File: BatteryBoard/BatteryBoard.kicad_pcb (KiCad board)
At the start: 4 copper layers, 45 x 44 mm, 67 parts, among them J1 M55-7102642R, Q1 PMPB13XNE,115, Q2 PMPB13XNE,115, Q3 PMPB13XNE,115, Q5 PMPB13XNE,115, U1 INA185A4IDRLR, U10 SI3477DV-T1-GE3, U13 TPS259472ARPWR, U2 SI3477DV-T1-GE3, U6 TPS63802DLAR, U8 BQ25756ERRVR

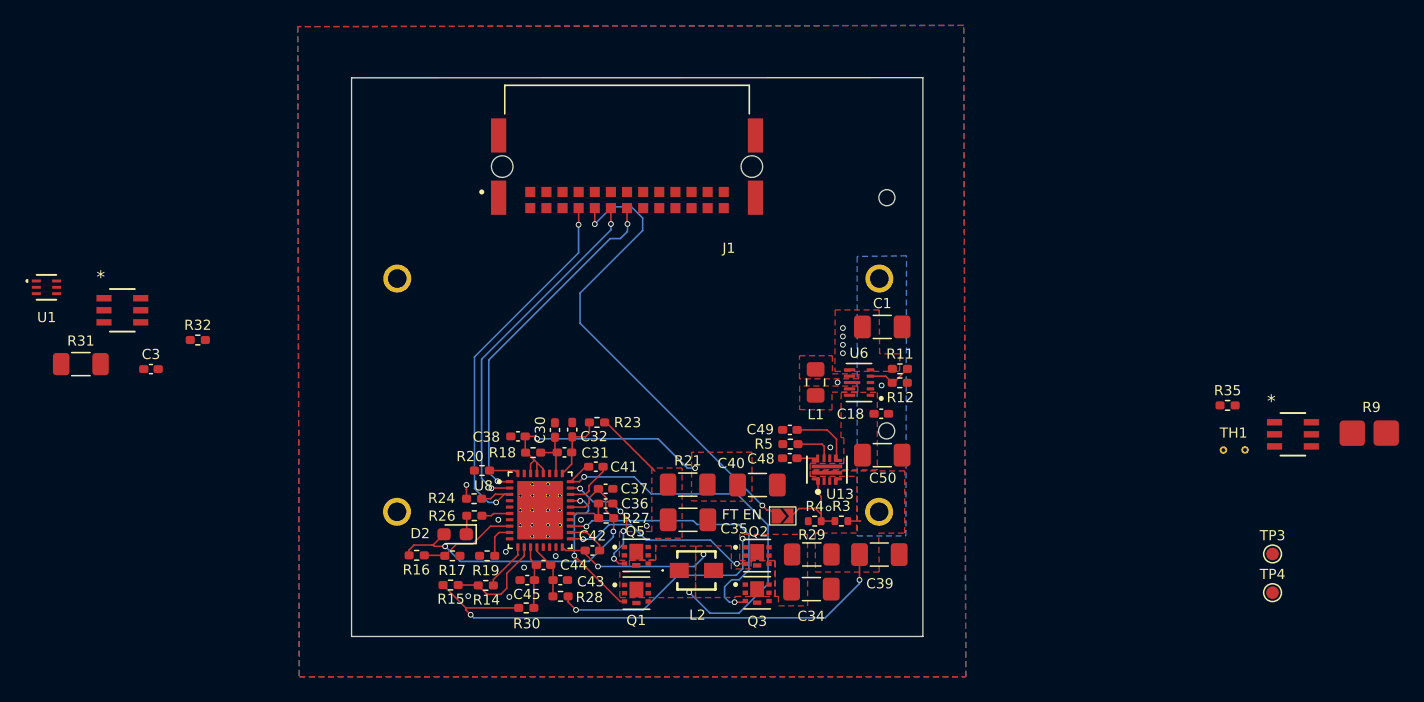
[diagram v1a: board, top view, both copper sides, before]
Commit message: Routing and schematic work on most boards
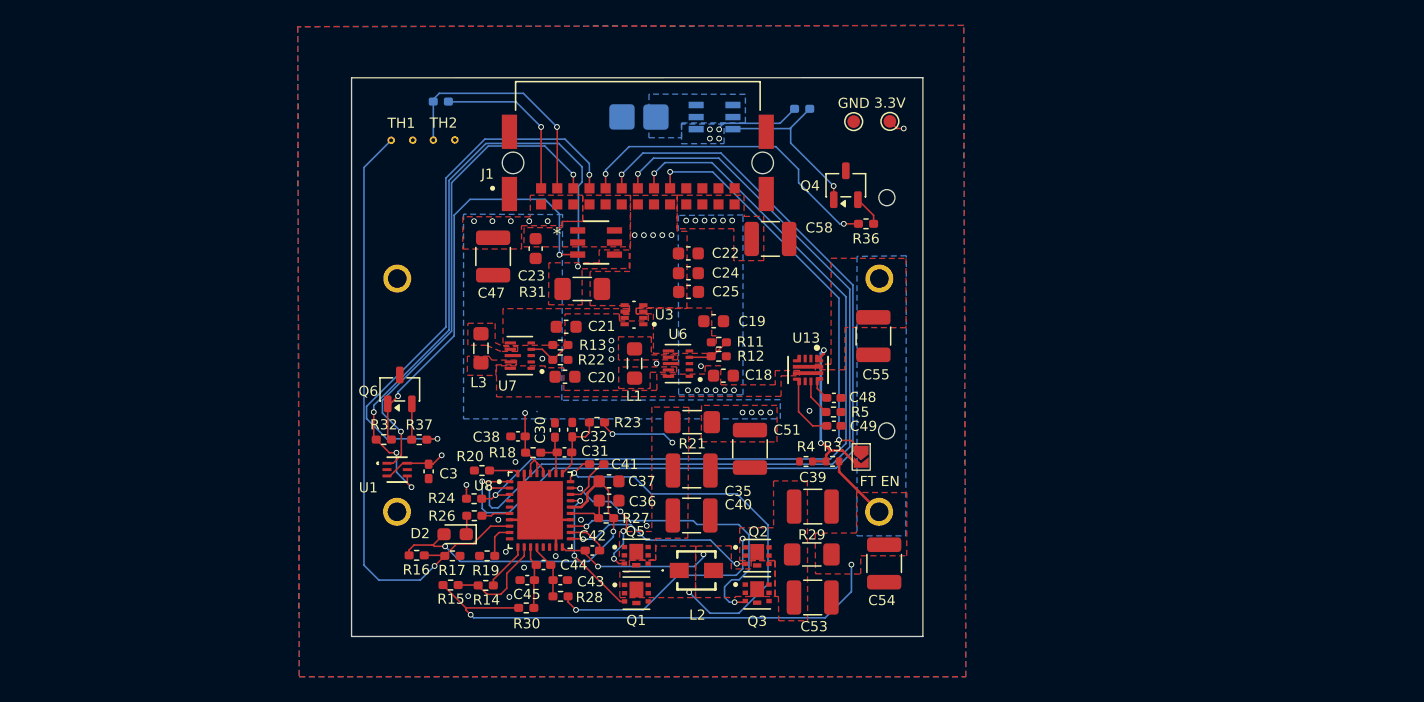
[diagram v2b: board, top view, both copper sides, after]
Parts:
- removed C1, C34, C50: 47uF, Capacitor_SMD:C_1206_3216Metric_Pad1.33x1.80mm_HandSolder
- added C19: 10uF, Capacitor_SMD:C_0603_1608Metric, F.Cu at (97.9, 60.9)
- added C20: 10uF, Capacitor_SMD:C_0603_1608Metric, F.Cu at (86.2, 65.3)
- added C21: 10uF, Capacitor_SMD:C_0603_1608Metric, F.Cu at (86.3, 61.4)
- added C22: 10uF, Capacitor_SMD:C_0603_1608Metric, F.Cu at (95.9, 55.6)
- added C23: 10uF, Capacitor_SMD:C_0603_1608Metric, F.Cu at (83.9, 55.2)
- added C24: 10uF, Capacitor_SMD:C_0603_1608Metric, F.Cu at (95.9, 57.1)
- added C25: 10uF, Capacitor_SMD:C_0603_1608Metric, F.Cu at (95.9, 58.6)
- added C47: 22uF, Capacitor_SMD:C_1210_3225Metric, F.Cu at (80.5, 55.8)
- added C51: 22uF, Capacitor_SMD:C_1210_3225Metric, F.Cu at (100.8, 71.0)
- added C53: 22uF, Capacitor_SMD:C_1210_3225Metric, F.Cu at (105.7, 82.7)
- added C54: 22uF, Capacitor_SMD:C_1210_3225Metric, F.Cu at (111.3, 80.0)
- added C55: 22uF, Capacitor_SMD:C_1210_3225Metric, F.Cu at (110.5, 62.1)
- added C58: 22uF, Capacitor_SMD:C_1210_3225Metric, F.Cu at (102.4, 54.5)
- added L3: 470nH, Inductor_SMD:L_0805_2012Metric_Pad1.05x1.20mm_HandSolder, F.Cu at (79.6, 63.1)
- added Q4: T2N7002AK,LM, Package_TO_SOT_SMD:SOT-23-3, F.Cu at (108.3, 50.2)
- added Q6: T2N7002AK,LM, Package_TO_SOT_SMD:SOT-23-3, F.Cu at (73.2, 66.3)
- added R13: 280k, Resistor_SMD:R_0402_1005Metric_Pad0.72x0.64mm_HandSolder, F.Cu at (85.8, 62.8)
- added R22: 50k, Resistor_SMD:R_0402_1005Metric_Pad0.72x0.64mm_HandSolder, F.Cu at (85.8, 64.0)
- added R36: 100, Resistor_SMD:R_0402_1005Metric_Pad0.72x0.64mm_HandSolder, F.Cu at (109.9, 53.3)
- added R37: 100, Resistor_SMD:R_0402_1005Metric_Pad0.72x0.64mm_HandSolder, F.Cu at (74.7, 70.3)
- added R38: 10k, Resistor_SMD:R_0402_1005Metric_Pad0.72x0.64mm_HandSolder, B.Cu at (76.4, 43.6)
- added TH2: NRBG104F3435B2F, inspirefly:NRBG104F3435B2F, F.Cu at (76.7, 47.0)
- added U3: TPS2117DRLR, inspirefly:SOTFL50P160X60-8N, F.Cu at (91.6, 60.4)
- added U7: TPS63802DLAR, inspirefly:VREG_TPS63802DLAR, F.Cu at (82.7, 63.6)
- C18, C36, C37: footprint Capacitor_SMD:C_0402_1005Metric_Pad0.74x0.62mm_HandSolder -> Capacitor_SMD:C_0603_1608Metric
- C35, C39, C40: value 47uF -> 22uF; footprint Capacitor_SMD:C_1206_3216Metric_Pad1.33x1.80mm_HandSolder -> Capacitor_SMD:C_1210_3225Metric
- L1: footprint Inductor_SMD:L_0805_2012Metric_Pad1.15x1.40mm_HandSolder -> Inductor_SMD:L_0805_2012Metric_Pad1.05x1.20mm_HandSolder
- R3: value 143k -> 649k
- R32: value 100k -> 10k
- R35: value 100k -> 10k; moved to B.Cu
- R4: value 100k -> 348k
- R5: value 1k -> 750
- R9, U2: moved to B.Cu
- moved TH1 69.9 mm to (73.4, 47.0)
- moved R9 62.7 mm to (92.0, 45.8), turned to 180 degrees
- moved U2 52.0 mm to (98.0, 44.9), turned to 180 degrees
- moved GND 49.6 mm to (109.0, 45.2)
- moved 3.3V 45.5 mm to (111.8, 45.2)
- moved R35 40.8 mm to (104.9, 44.2), turned to 180 degrees
- moved R31 39.9 mm to (87.6, 58.4), turned to 180 degrees
- moved U10 37.7 mm to (88.7, 54.7)
- moved U1 31.1 mm to (73.0, 72.6)
- moved C3 23.3 mm to (75.5, 72.8), turned to 90 degrees
- moved R32 16.6 mm to (71.9, 70.2)
- moved R11 14.4 mm to (98.3, 62.6)
- moved R12 14.4 mm to (98.3, 63.7)
- moved L1 14.3 mm to (91.7, 64.3)
- moved U6 14.3 mm to (95.1, 64.3)
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- renumbered TP3 to 3.3V, TP4 to GND
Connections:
- net EXTERNAL_3.3V_CUTOFF renamed Net-(Q6-D)
- C39 pad 1: BAT+ -> Net-(C39-Pad1)
- C40 pad 1: EXTERNAL_VOLTAGE -> Net-(C35-Pad1)
- J1 pad A1: EXTERNAL_VOLTAGE -> EN_THERMISTOR_READ
- J1 pad A10: +3.3V -> GND
- J1 pad A11: +3.3V -> GND
- J1 pad A12: +3.3V -> GND
- J1 pad A13: +3.3V -> GND
- J1 pad A2: EXTERNAL_VOLTAGE -> ADC1_A2
- J1 pad A3: EXTERNAL_VOLTAGE -> ADC1_A1
- J1 pad A4: EXTERNAL_VOLTAGE -> PAYLOAD_3.3V_EN
- J1 pad A5: GND -> BAT_HEAT_EN
- J1 pad A6: GND -> I2C2_SCL
- J1 pad A7: GND -> I2C2_SDA
- J1 pad A8: GND -> BATMANG_INT_DIN
- J1 pad A9: GND -> FOOTSWITCH
- J1 pad B1: PAYLOAD_3.3V -> EXTERNAL_VOLTAGE
- J1 pad B10: BAT_VOLTAGE -> PROTECTED_VOLTAGE
- J1 pad B11: BAT_VOLTAGE -> PROTECTED_VOLTAGE
- J1 pad B12: BAT_VOLTAGE -> PROTECTED_VOLTAGE
- J1 pad B13: BAT_VOLTAGE -> PROTECTED_VOLTAGE
- J1 pad B2: PAYLOAD_3.3V -> EXTERNAL_VOLTAGE
- J1 pad B3: PAYLOAD_3.3V -> EXTERNAL_VOLTAGE
- J1 pad B4: BATMANG_INT_DIN -> PAYLOAD_3.3V
- J1 pad B5: FOOTSWITCH -> PAYLOAD_3.3V
- J1 pad B6: I2C2_SDA -> PAYLOAD_3.3V
- J1 pad B7: I2C2_SCL -> +3.3V
- J1 pad B8: BAT_HEAT_EN -> +3.3V
- J1 pad B9: PAYLOAD_3.3V_EN -> +3.3V
- Q2 pad 1: Net-(C34-Pad1) -> Net-(C39-Pad1)
- Q2 pad 2: Net-(C34-Pad1) -> Net-(C39-Pad1)
- Q2 pad 5: Net-(C34-Pad1) -> Net-(C39-Pad1)
- Q2 pad 6: Net-(C34-Pad1) -> Net-(C39-Pad1)
- Q2 pad 7: Net-(C34-Pad1) -> Net-(C39-Pad1)
- R11 pad 1: +3.3V -> Net-(U3-VIN1)
- R28 pad 2: Net-(C34-Pad1) -> Net-(C39-Pad1)
- R29 pad 1: Net-(C34-Pad1) -> Net-(C39-Pad1)
- R35 pad 1: BAT_HEAT_EN -> Net-(Q4-D)
- U10 pad 1: BOARD_OUT_3.3V -> PAYLOAD_3.3V
- U10 pad 2: BOARD_OUT_3.3V -> PAYLOAD_3.3V
- U10 pad 5: BOARD_OUT_3.3V -> PAYLOAD_3.3V
- U10 pad 6: BOARD_OUT_3.3V -> PAYLOAD_3.3V
- U2 pad 3: BAT_HEAT_EN -> Net-(Q4-D)
- U6 pad 6: +3.3V -> Net-(U3-VIN1)
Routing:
- net Net-(U1-IN-): track 0.00 -> 49.6 mm, vias 0 -> 4
- net I2C2_SCL: track 27.8 -> 73.0 mm
- net PAYLOAD_3.3V_EN: track 0.00 -> 44.0 mm, vias 0 -> 2
- net THERMISTOR_FEEDBACK: track 7.71 -> 49.7 mm, vias 0 -> 1
- net I2C2_SDA: track 28.1 -> 68.5 mm
- net ADC1_A1: track 0.00 -> 38.5 mm, vias 0 -> 2
- net Net-(Q6-D): track 0.00 -> 34.0 mm, vias 0 -> 2
- net BATMANG_INT_DIN: track 31.3 -> 64.2 mm
- net BAT_HEAT_EN: track 0.00 -> 25.2 mm, vias 0 -> 2
- net ADC1_A2: track 0.00 -> 19.1 mm, vias 0 -> 1
- net Net-(C39-Pad1): track 0.00 -> 18.2 mm, vias 0 -> 2
- net Net-(C34-Pad1): track 18.2 -> 0.00 mm, vias 2 -> 0
- net Net-(Q4-D): track 0.00 -> 13.8 mm, vias 0 -> 1
- net EN_THERMISTOR_READ: track 0.00 -> 12.8 mm, vias 0 -> 1
- net EXTERNAL_VOLTAGE: track 20.0 -> 7.44 mm, vias 2 -> 10
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- added copper zone on B.Cu, net EXTERNAL_VOLTAGE
- added copper zone on F.Cu, net Net-(C39-Pad1)
- added copper zone on B.Cu, net Net-(R9-Pad1)
- added copper zone on F.Cu, net Net-(U1-IN-)
- added copper zone on F.Cu, net Net-(U3-VIN1)
- added copper zone on F.Cu, net Net-(U3-VIN2)
- added copper zone on F.Cu, net Net-(U7-L1)
- added copper zone on F.Cu, net Net-(U7-L2)
- added copper zone on F.Cu, net PAYLOAD_3.3V
- added copper zone on B.Cu, net PROTECTED_VOLTAGE
- added copper zone on In2.Cu, net PROTECTED_VOLTAGE
- removed copper zone on F.Cu, net Net-(C34-Pad1)

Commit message: Finalize board work + BOM work
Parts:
- added G***: LOGO, LOGO, F.Cu at (74.7, 49.3)
- L2: footprint inspirefly:IHLP1212BZEZ2R2M1Z -> inspirefly:IND_SRP4020FA-2R2M_BRN
- turned L2 to 0 degrees
- renumbered 3.3V to TP3, GND to TP4
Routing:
- net EXTERNAL_SIDE_INDUC: track 31.8 -> 33.5 mm
- net BAT_SIDE_INDUC: track 12.4 -> 13.9 mm
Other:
- board text added: "Battery Board PQ V0.1"
